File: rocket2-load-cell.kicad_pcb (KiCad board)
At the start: 2 copper layers, 69 x 67 mm, 41 parts, among them J1 SWD, J2 Screw_Terminal_01x02, U2 STM32F103C8Tx, U3 AMS1117-3.3, U4 UA7812CKCS, Y1 16MHz

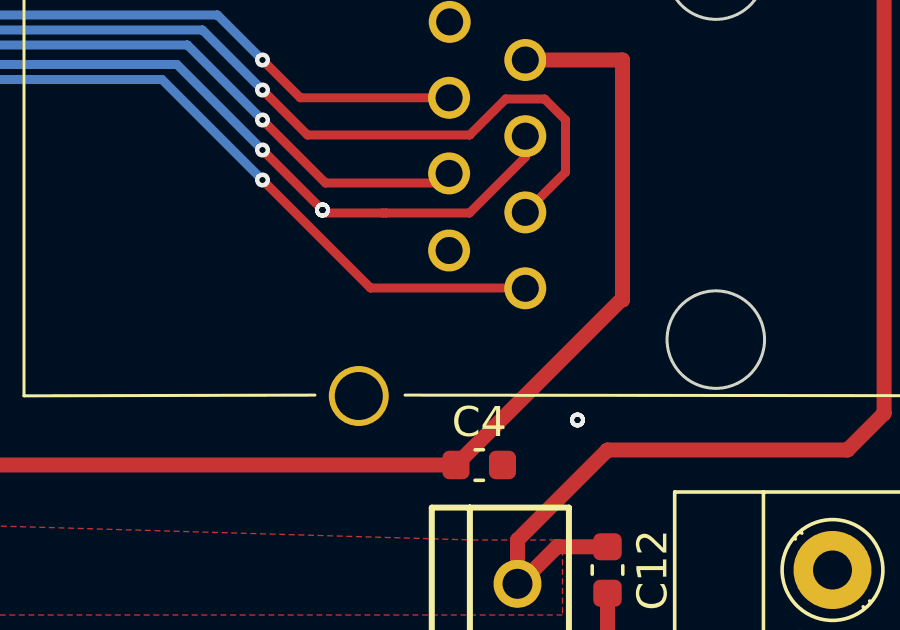
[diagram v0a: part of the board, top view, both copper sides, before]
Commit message: cleaned up vias once again removed redundant tracks
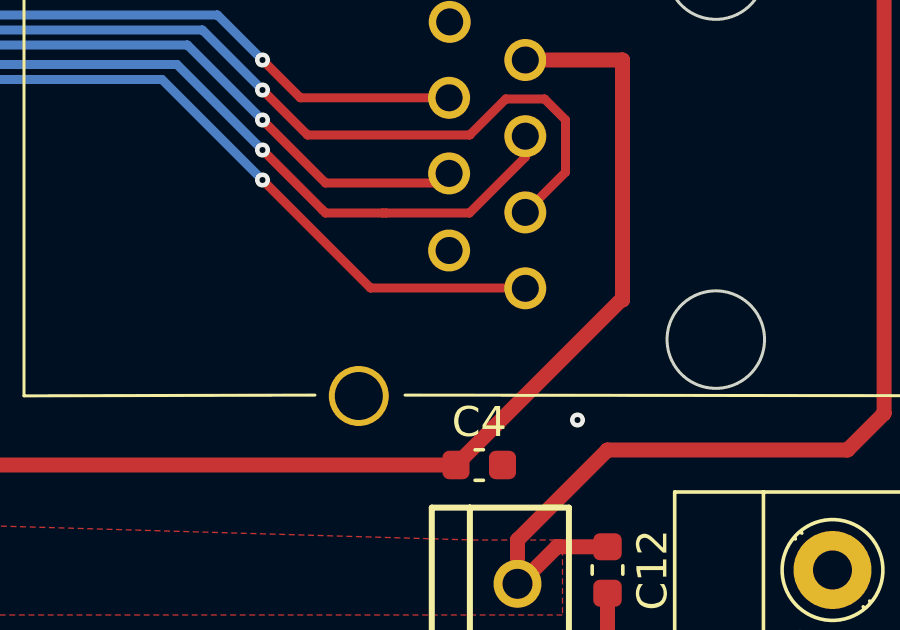
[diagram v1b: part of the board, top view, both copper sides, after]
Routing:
- net GND: vias 19 -> 18
- net ETH_TX: vias 5 -> 2
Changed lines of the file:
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@@
+	)
+	(via
+		(at 187 106.5)
+		(size 0.5)
+		(drill 0.2)
+		(layers "F.Cu" "B.Cu")
+		(net 2)
 	)
 	(via
@@
 	)
 	(via
-		(at 187 106.5)
-		(size 0.5)
-		(drill 0.2)
-		(layers "F.Cu" "B.Cu")
-		(net 2)
-	)
-	(via
-		(at 174 124)
-		(size 0.5)
-		(drill 0.2)
-		(layers "F.Cu" "B.Cu")
-		(free yes)
-		(net 2)
-	)
-	(via
 		(at 128.8375 113.75)
 		(size 0.5)
@@
 	)
 	(via
-		(at 165.5 117)
-		(size 0.5)
-		(drill 0.2)
-		(layers "F.Cu" "B.Cu")
-		(net 52)
-	)
-	(via
 		(at 138.5 112.5)
 		(size 0.5)
 		(drill 0.2)
-		(layers "F.Cu" "B.Cu")
-		(net 52)
-	)
-	(via
-		(at 165.5 117)
-		(size 0.5)
-		(drill 0.2)
-		(layers "F.Cu" "B.Cu")
-		(net 52)
-	)
-	(via
-		(at 165.5 117)
-		(size 0.5)
-		(drill 0.2)

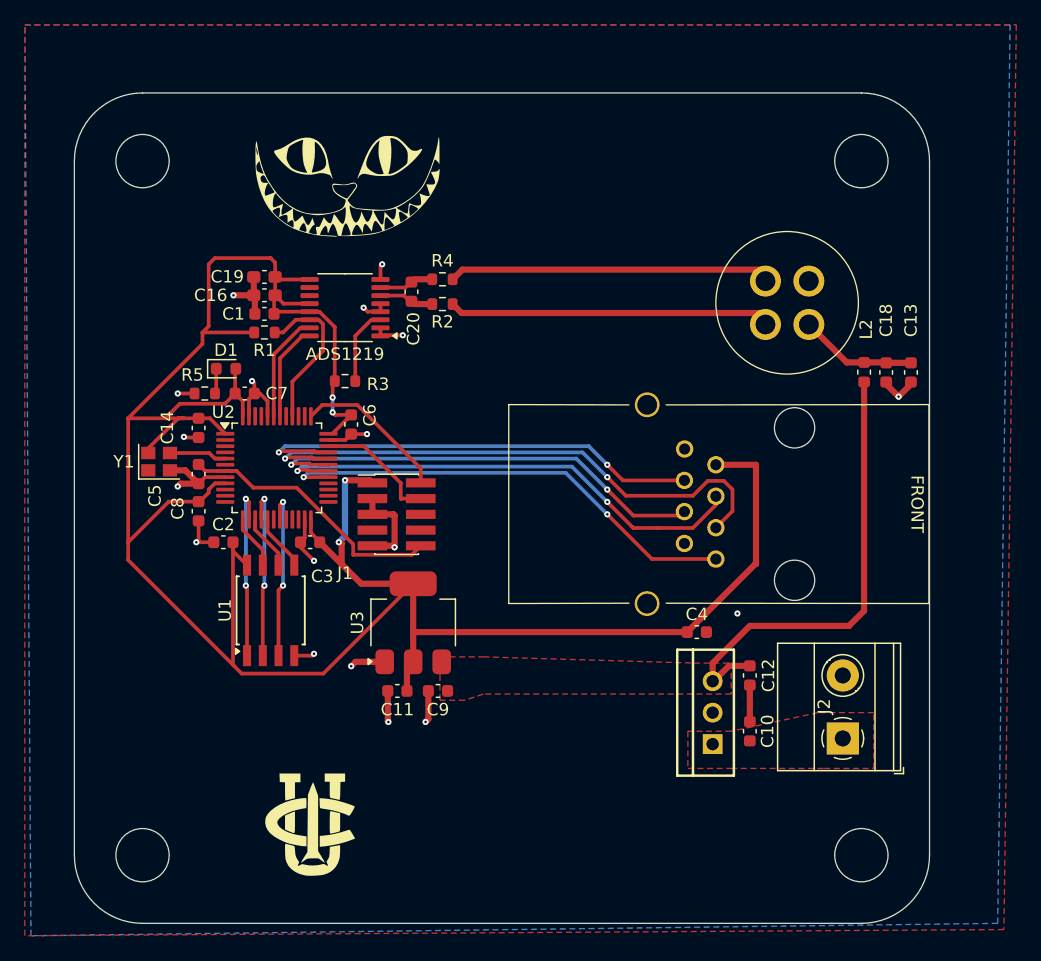
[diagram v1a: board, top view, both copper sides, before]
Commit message: moved gx12 futher from ethernet
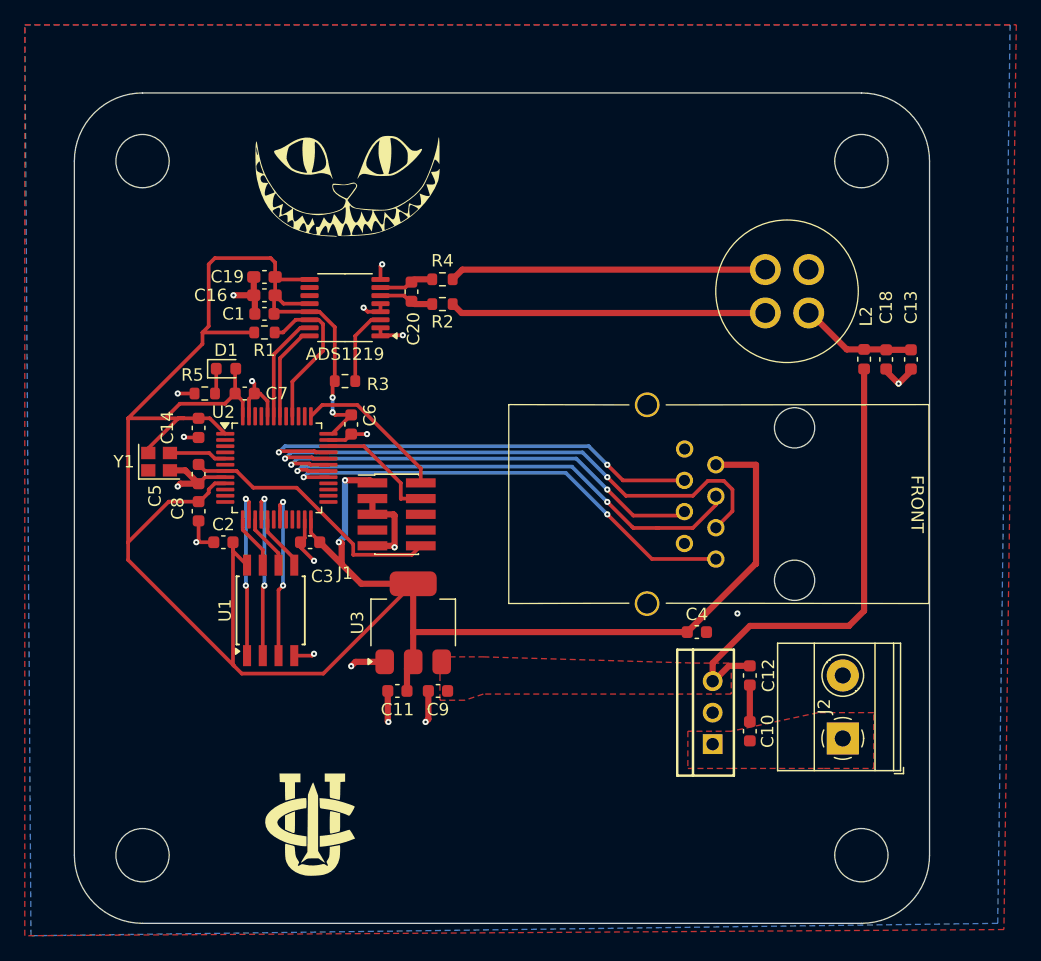
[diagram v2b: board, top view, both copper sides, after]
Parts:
- moved C13 1.05 mm to (188.0, 103.5)
- moved C18 1.05 mm to (186.0, 103.5)
- moved L2 1.05 mm to (184.2, 103.5)
- moved GX12 0.93 mm to (178.0, 98.0)
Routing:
- net VBUS: track 37.4 -> 38.4 mm
- net ADS_CLK: track 8.49 -> 7.92 mm
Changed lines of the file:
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@@
 	(footprint "Capacitor_SMD:C_0603_1608Metric"
 		(layer "F.Cu")
-		(at 188 104.55 -90)
+		(at 188 103.5 -90)
 		(descr "Capacitor SMD 0603 (1608 Metric), square (rectangular) end terminal, IPC_7351 nominal, (Body size source: IPC-SM-782 page 76, https://www.pcb-3d.com/wordpress/wp-content/uploads/ipc-sm-782a_amendment_1_and_2.pdf), generated with kicad-footprint-generator")
 		(tags "capacitor")
@@
 	(footprint "Inductor_SMD:L_0603_1608Metric"
 		(layer "F.Cu")
-		(at 184.22 104.53 -90)
+		(at 184.22 103.48 -90)
 		(descr "Inductor SMD 0603 (1608 Metric), square (rectangular) end terminal, IPC_7351 nominal, (Body size source: http://www.tortai-tech.com/upload/download/2011102023233369053.pdf), generated with kicad-footprint-generator")
 		(tags "inductor")
@@
 	(footprint "UCIRP-KiCAD-Lib:gx12"
 		(layer "F.Cu")
-		(at 178.01 98.93 180)
+		(at 178 98 180)
 		(property "Reference" "GX12"
 			(at 0 -0.5 180)
@@
 			)
 			(rotate
-				(xyz -90 0 0)
+				(xyz -90 0 90)
 			)
 		)
@@
 	(footprint "Capacitor_SMD:C_0603_1608Metric"
 		(layer "F.Cu")
-		(at 186 104.55 -90)
+		(at 186 103.5 -90)
 		(descr "Capacitor SMD 0603 (1608 Metric), square (rectangular) end terminal, IPC_7351 nominal, (Body size source: IPC-SM-782 page 76, https://www.pcb-3d.com/wordpress/wp-content/uploads/ipc-sm-782a_amendment_1_and_2.pdf), generated with kicad-footprint-generator")
 		(tags "capacitor")
@@
 	)
 	(segment
-		(start 145.250734 101.549266)
-		(end 145.2 101.6)
-		(width 0.3)
-		(layer "F.Cu")
-		(net 2)
-	)
-	(segment
 		(start 134.975 98.325)
 		(end 133.3375 98.325)
@@
 	)
 	(segment
-		(start 187 106.5)
-		(end 188 105.5)
+		(start 187 105.45)
+		(end 188 104.45)
 		(width 0.5)
 		(layer "F.Cu")
@@
 	)
 	(segment
-		(start 187 106.5)
-		(end 186 105.5)
+		(start 187 105.45)
+		(end 186 104.45)
 		(width 0.5)
 		(layer "F.Cu")
@@
 	)
 	(via
-		(at 187 106.5)
+		(at 187 105.45)
 		(size 0.5)
 		(drill 0.2)
@@
 	)
 	(segment
-		(start 175 125)
-		(end 183 125)
+		(start 172 128)
+		(end 172 129.46)
 		(width 0.5)
 		(layer "F.Cu")
@@
 	)
 	(segment
-		(start 172 128)
-		(end 175 125)
+		(start 184.22 123.78)
+		(end 183 125)
 		(width 0.5)
 		(layer "F.Cu")
@@
 	)
 	(segment
-		(start 184.22 123.78)
-		(end 184.22 105.3175)
+		(start 184.22 104.2675)
+		(end 184.22 123.78)
 		(width 0.5)
 		(layer "F.Cu")
@@
 	)
 	(segment
-		(start 172 129.46)
+		(start 175 125)
 		(end 172 128)
 		(width 0.5)
@@
 	(segment
 		(start 183 125)
-		(end 184.22 123.78)
+		(end 175 125)
 		(width 0.5)
 		(layer "F.Cu")
@@
 	)
 	(segment
-		(start 184.22 103.7425)
-		(end 185.9675 103.7425)
+		(start 184.22 102.6925)
+		(end 185.9675 102.6925)
 		(width 0.5)
 		(layer "F.Cu")
@@
 	)
 	(segment
-		(start 186 103.775)
-		(end 188 103.775)
+		(start 186 102.725)
+		(end 188 102.725)
 		(width 0.5)
 		(layer "F.Cu")
@@
 	)
 	(segment
-		(start 184.22 103.7425)
-		(end 182.8225 103.7425)
+		(start 184.22 102.6925)
+		(end 182.8225 102.6925)
 		(width 0.5)
 		(layer "F.Cu")
@@
 	)
 	(segment
-		(start 182.8225 103.7425)
-		(end 179.76 100.68)
+		(start 182.8225 102.6925)
+		(end 179.76 99.63)
 		(width 0.5)
 		(layer "F.Cu")
@@
 	)
 	(segment
-		(start 140.5625 101.889168)
-		(end 140.5625 100.650001)
-		(width 0.3)
-		(layer "F.Cu")
-		(net 16)
-	)
-	(segment
 		(start 138.0875 105.289168)
 		(end 140.5625 102.814168)
@@
 	(segment
 		(start 140.5625 102.814168)
-		(end 140.5625 101.889168)
+		(end 140.5625 100.650001)
 		(width 0.3)
 		(layer "F.Cu")
@@
 	)
 	(segment
-		(start 138.9 101.6)
-		(end 139.475 101.6)
-		(width 0.3)
-		(layer "F.Cu")
-		(net 44)
-	)
-	(segment

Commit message: changed back to 5v and removed 12 volt reg
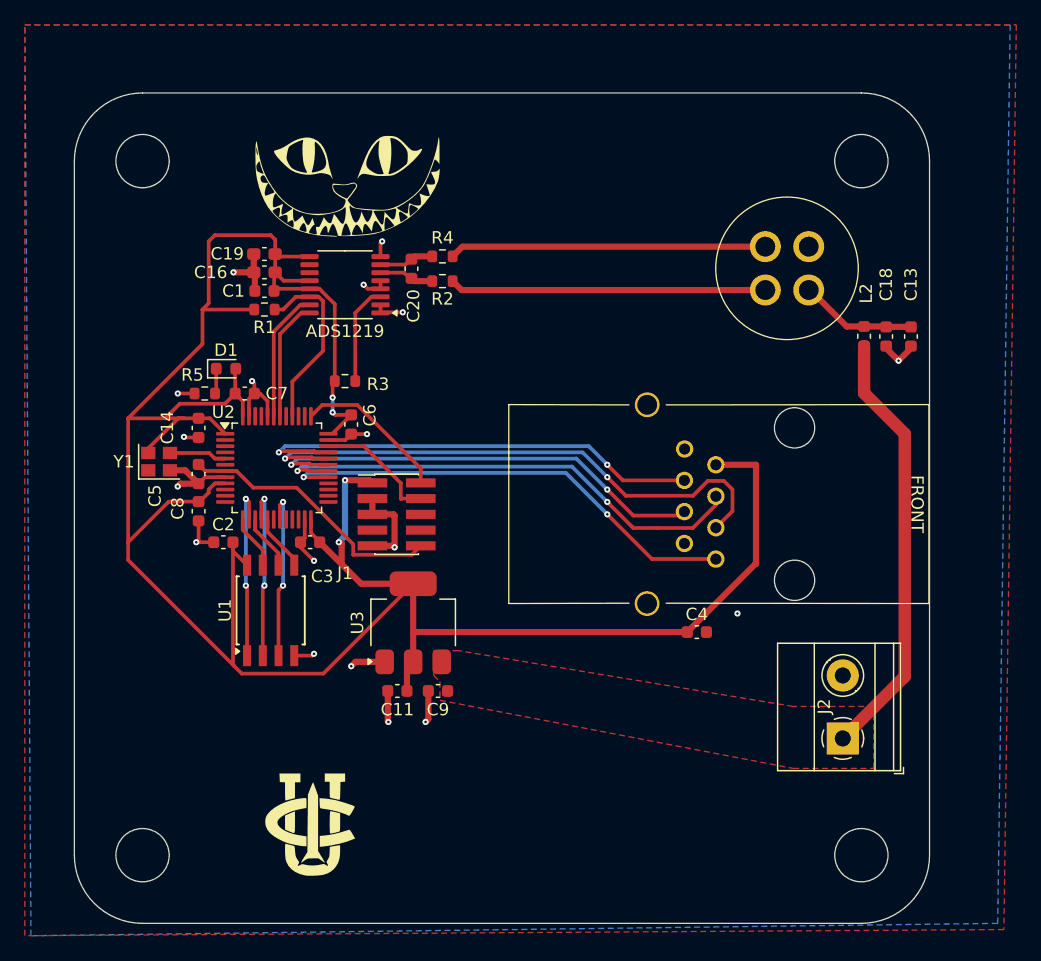
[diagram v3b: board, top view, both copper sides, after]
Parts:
- removed C10: .33uF, Capacitor_SMD:C_0603_1608Metric
- removed C12: .1uF, Capacitor_SMD:C_0603_1608Metric
- removed U4: UA7812CKCS, ucirp:KCS0003B
- moved ADS1219 1.85 mm to (142.3, 97.5)
- moved C1 1.85 mm to (135.8, 98.0)
- moved C16 1.85 mm to (135.8, 96.5)
- moved L2 1.85 mm to (184.2, 101.6)
- moved R1 1.85 mm to (135.8, 99.5)
- moved C13 1.85 mm to (188.0, 101.7)
- moved C18 1.85 mm to (186.0, 101.7)
- moved C19 1.85 mm to (135.8, 95.0)
- moved C20 1.85 mm to (147.7, 96.2)
- moved GX12 1.85 mm to (178.0, 96.2)
- moved R2 1.85 mm to (150.2, 97.2)
- moved R4 1.85 mm to (150.2, 95.2)
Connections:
- J2 pad 1: VIN -> VBUS
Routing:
- net +3.3V: track 206.7 -> 210.4 mm
- net VBUS: track 38.4 -> 35.1 mm
- net GND: track 58.8 -> 55.9 mm
- net ADS_DATA: track 8.77 -> 10.6 mm
- net Net-(ADS1219-RESET): track 6.23 -> 8.08 mm
- net ADS_DRDY: track 12.9 -> 14.8 mm
- net ADS_CLK: track 7.92 -> 9.72 mm
- removed copper zone on F.Cu, net VIN
